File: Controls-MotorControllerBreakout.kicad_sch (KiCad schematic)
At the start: 13 parts, among them J1 MC CAN 1, J2 MC CAN 2, J3 CTRLS, J4 EXT PWR, J5 CANDAPTER

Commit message: start layouting again
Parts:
- removed LOGO2: WS Motor Interface, Wavesculptor_Motor_Interface:Wavesculptor_Motor_Interface_Type_1, symbol utsvt-misc:Logo_Placeholder
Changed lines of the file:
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@@
-	)
-	(symbol
-		(lib_id "utsvt-misc:Logo_Placeholder")
-		(at 127 83.82 0)
-		(unit 1)
-		(exclude_from_sim no)
-		(in_bom yes)
-		(on_board yes)
-		(dnp no)
-		(fields_autoplaced yes)
-		(property "Reference" "LOGO2"
-			(at 127 80.01 0)
-			(effects
-				(font
-					(size 1.27 1.27)
-				)
-				(hide yes)
-			)
-		)
-		(property "Value" "WS Motor Interface"
-			(at 130.81 83.8199 0)
-			(effects
-				(font
-					(size 1.27 1.27)
-				)
-				(justify left)
-			)
-		)
-		(property "Footprint" "Wavesculptor_Motor_Interface:Wavesculptor_Motor_Interface_Type_1"
-			(at 127 81.915 0)
-			(effects
-				(font
-					(size 1.27 1.27)
-				)
-				(hide yes)
-			)
-		)
-		(property "Datasheet" ""
-			(at 127 81.915 0)
-			(effects
-				(font
-					(size 1.27 1.27)
-				)
-				(hide yes)
-			)
-		)
-		(property "Description" "Graph footprint placeholder"
-			(at 127 83.82 0)
-			(effects
-				(font
-					(size 1.27 1.27)
-				)
-				(hide yes)
-			)
-		)
-		(property "Sim.Device" ""
-			(at 127 83.82 0)
-			(effects
-				(font
-					(size 1.27 1.27)
-				)
-				(hide yes)
-			)
-		)
-		(property "Sim.Pins" ""
-			(at 127 83.82 0)
-			(effects
-				(font
-					(size 1.27 1.27)
-				)
-				(hide yes)
-			)
-		)
-		(instances
-			(project "Controls-MotorControllerBreakout"
-				(path "/0a971d65-5373-49c6-bc07-3a5d4263dbef"
-					(reference "LOGO2")
-					(unit 1)
-				)
-			)
-		)
 	)
 	(symbol

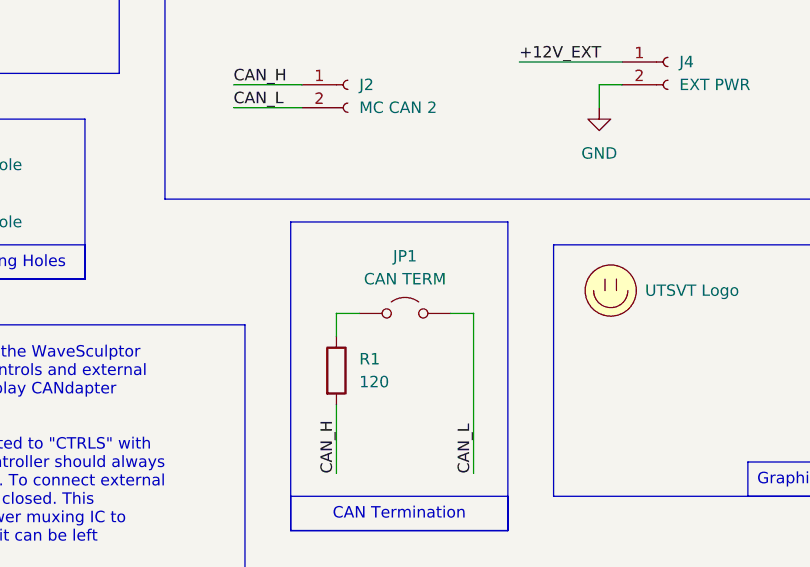
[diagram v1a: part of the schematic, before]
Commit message: output fuse and solder jumpers
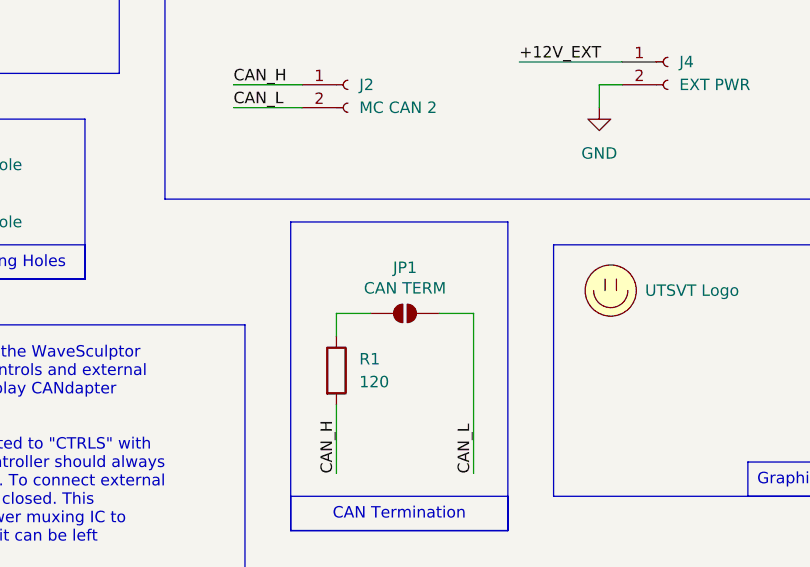
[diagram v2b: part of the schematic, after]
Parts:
- JP1: footprint Connector_PinHeader_2.54mm:PinHeader_1x02_P2.54mm_Vertical -> Jumper:SolderJumper-2_P1.3mm_Open_RoundedPad1.0x1.5mm; symbol Jumper:Jumper_2_Open -> Jumper:SolderJumper_2_Open; now left out of the parts list
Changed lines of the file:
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@@
-	(wire
-		(pts
-			(xy 111.76 78.74) (xy 109.22 78.74)
-		)
-		(stroke
-			(width 0)
-			(type default)
-		)
-	)
 	(wire
 		(pts
@@
 	(wire
 		(pts
-			(xy 96.52 78.74) (xy 99.06 78.74)
+			(xy 96.52 78.74) (xy 100.33 78.74)
 		)
 		(stroke
@@
 		(pts
 			(xy 85.09 55.88) (xy 92.71 55.88)
+		)
+		(stroke
+			(width 0)
+			(type default)
+		)
+	)
+	(wire
+		(pts
+			(xy 107.95 78.74) (xy 111.76 78.74)
 		)
 		(stroke
@@
 	)
 	(symbol
-		(lib_id "Jumper:Jumper_2_Open")
+		(lib_id "Jumper:SolderJumper_2_Open")
 		(at 104.14 78.74 0)
 		(unit 1)
 		(exclude_from_sim yes)
-		(in_bom yes)
+		(in_bom no)
 		(on_board yes)
 		(dnp no)
-		(fields_autoplaced yes)
 		(property "Reference" "JP1"
-			(at 104.14 72.39 0)
+			(at 104.14 73.66 0)
 			(effects
 				(font
@@
 		)
 		(property "Value" "CAN TERM"
-			(at 104.14 74.93 0)
-			(effects
-				(font
-					(size 1.27 1.27)
-				)
-			)
-		)
-		(property "Footprint" "Connector_PinHeader_2.54mm:PinHeader_1x02_P2.54mm_Vertical"
+			(at 104.14 75.946 0)
+			(effects
+				(font
+					(size 1.27 1.27)
+				)
+			)
+		)
+		(property "Footprint" "Jumper:SolderJumper-2_P1.3mm_Open_RoundedPad1.0x1.5mm"
 			(at 104.14 78.74 0)
 			(effects
@@
 			)
 		)
-		(property "Description" "Jumper, 2-pole, open"
+		(property "Description" "Solder Jumper, 2-pole, open"
 			(at 104.14 78.74 0)
 			(effects

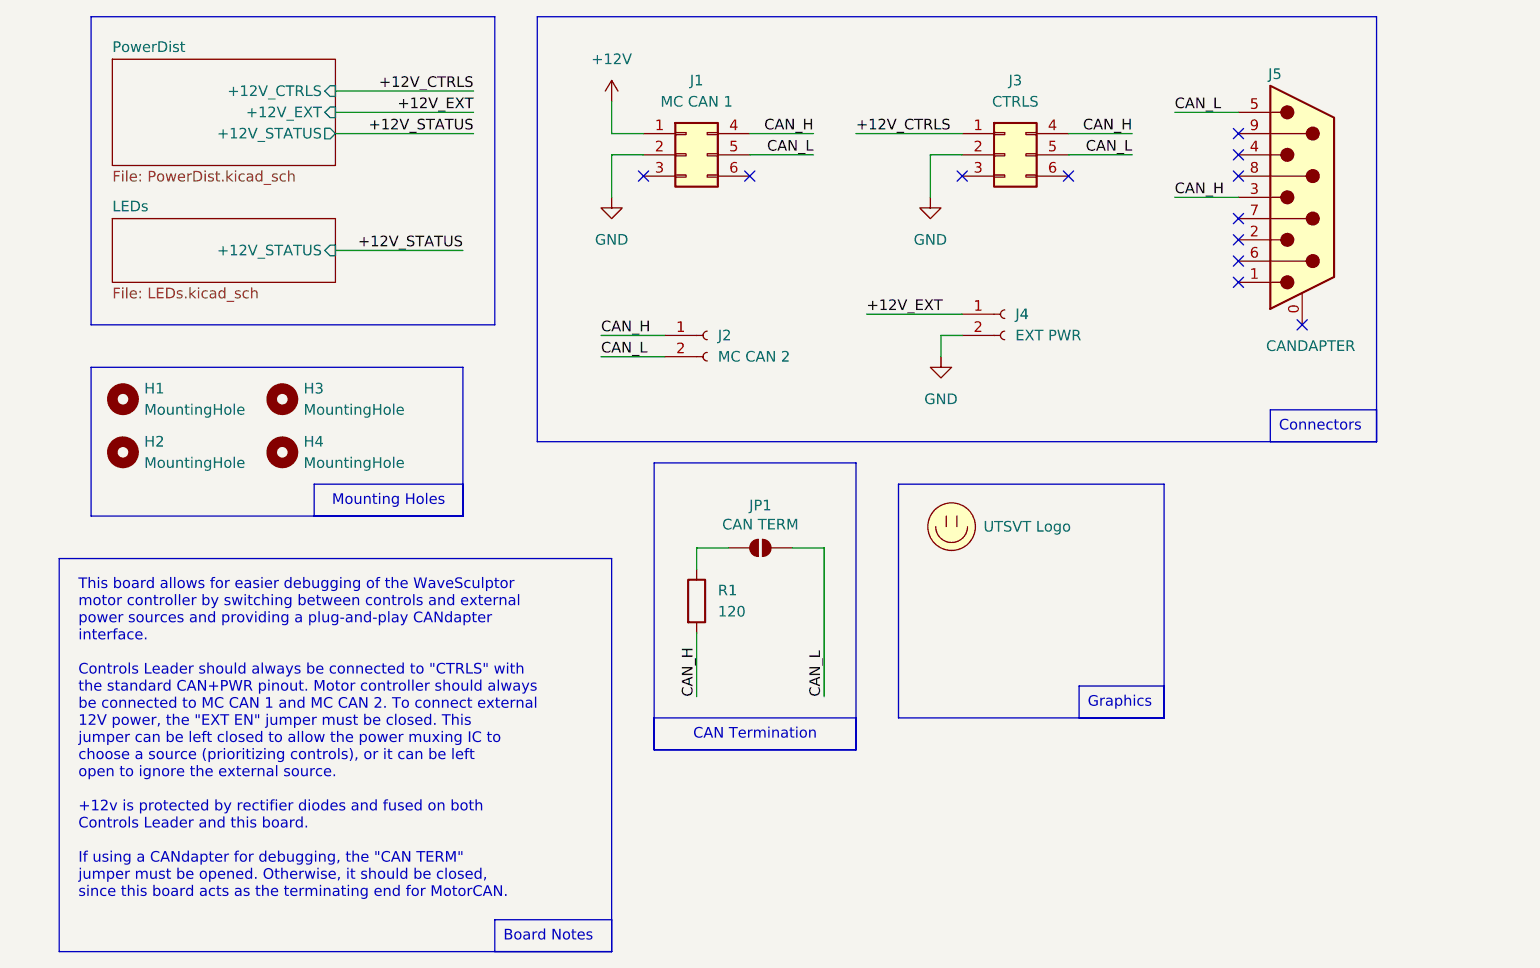
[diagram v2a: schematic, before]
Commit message: add fan conns, layout + routing
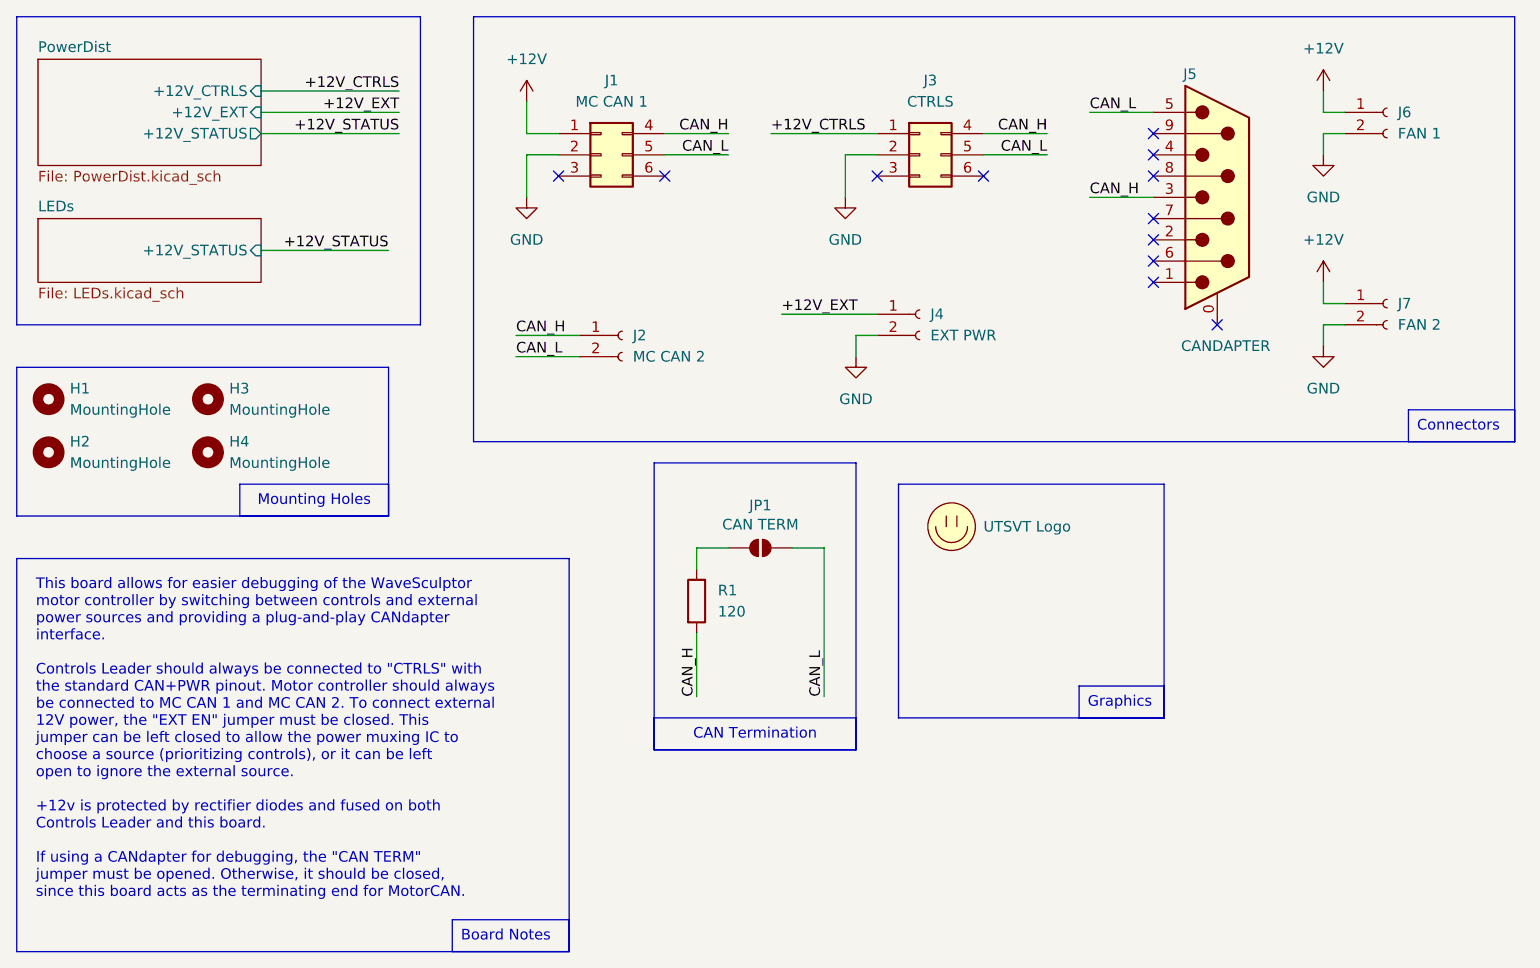
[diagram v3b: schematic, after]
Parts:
- added J6: FAN 1, Connector_Molex:Molex_Micro-Fit_3.0_43650-0215_1x02_P3.00mm_Vertical, symbol Connector:Conn_01x02_Socket
- added J7: FAN 2, Connector_Molex:Molex_Micro-Fit_3.0_43650-0215_1x02_P3.00mm_Vertical, symbol Connector:Conn_01x02_Socket
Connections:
- net +12V: now also J6.1 (Pin_1), J7.1 (Pin_1)
- net GND: now also J6.2 (Pin_2), J7.2 (Pin_2)
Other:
- moved on the sheet: H1, H2, H3, H4, J1, J2, J3, J4, J5

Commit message: gerbs, BOM
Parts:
- J6, J7: P/N (none) -> 0436500215
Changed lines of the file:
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@@
+			)
+		)
+		(property "P/N" "0436500215"
+			(at 179.07 26.67 0)
+			(effects
+				(font
+					(size 1.27 1.27)
+				)
+				(hide yes)
 			)
 		)
@@
 			(at 179.07 49.53 0)
 			(effects
+				(font
+					(size 1.27 1.27)
+				)
+				(hide yes)
+			)
+		)
+		(property "P/N" "0436500215"
+			(at 179.07 49.53 0)
+			(effects

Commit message: flyback sch
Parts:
- added D6: FLYBK1, symbol Device:D
- added D7: FLYBK2, symbol Device:D
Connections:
- net +12V: now also D6.1 (K), D7.1 (K)
- net GND: now also D6.2 (A), D7.2 (A)
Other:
- moved on the sheet: J5, J6, J7

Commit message: hi its me again
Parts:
- D6, D7: footprint (none) -> UTSVT_Passive:DO-221AC; symbol Device:D -> Device:D_Schottky; P/N (none) -> VSSAF522-M3/H
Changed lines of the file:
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@@
 		(title "Controls - Motor Controller Breakout")
 		(date "2024-12-22")
-		(rev "v2.0")
+		(rev "v2.1")
 		(company "LHRS")
 	)
@@
 	)
 	(symbol
-		(lib_id "Device:D")
+		(lib_id "Device:D_Schottky")
 		(at 163.83 85.09 270)
 		(unit 1)
@@
 		(fields_autoplaced yes)
 		(property "Reference" "D6"
-			(at 166.37 83.8199 90)
+			(at 166.37 83.5024 90)
 			(effects
 				(font
@@
 		)
 		(property "Value" "FLYBK1"
-			(at 166.37 86.3599 90)
+			(at 166.37 86.0424 90)
 			(effects
 				(font
@@
 			)
 		)
-		(property "Footprint" ""
+		(property "Footprint" "UTSVT_Passive:DO-221AC"
 			(at 163.83 85.09 0)
 			(effects
@@
 			)
 		)
-		(property "Description" "Diode"
+		(property "Description" "Schottky diode"
 			(at 163.83 85.09 0)
 			(effects
@@
 		(property "Sim.Pins" "1=K 2=A"
 			(at 163.83 85.09 0)
+			(effects
+				(font
+					(size 1.27 1.27)
+				)
+				(hide yes)
+			)
+		)
+		(property "P/N" "VSSAF522-M3/H"
+			(at 163.83 85.09 90)
 			(effects
 				(font
@@
 	)
 	(symbol
-		(lib_id "Device:D")
+		(lib_id "Device:D_Schottky")
 		(at 177.8 85.09 270)
 		(unit 1)
@@
 		(fields_autoplaced yes)
 		(property "Reference" "D7"
-			(at 180.34 83.8199 90)
+			(at 180.34 83.5024 90)
 			(effects
 				(font
@@
 		)
 		(property "Value" "FLYBK2"
-			(at 180.34 86.3599 90)
+			(at 180.34 86.0424 90)
 			(effects
 				(font
@@
 			)
 		)
-		(property "Footprint" ""
+		(property "Footprint" "UTSVT_Passive:DO-221AC"
 			(at 177.8 85.09 0)
 			(effects
@@
 			)
 		)
-		(property "Description" "Diode"
+		(property "Description" "Schottky diode"
 			(at 177.8 85.09 0)
 			(effects
@@
 			(effects
 				(font
+					(size 1.27 1.27)
+				)
+				(hide yes)
+			)
+		)
+		(property "P/N" "VSSAF522-M3/H"
+			(at 177.8 85.09 90)
+			(effects
+				(font
